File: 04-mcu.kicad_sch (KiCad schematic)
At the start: 16 parts, among them J4 USB-C, J5 microSD_PushPush, SW1 RESET, SW2 BOOT, U6 ESP32-S3-WROOM-1-N8R2

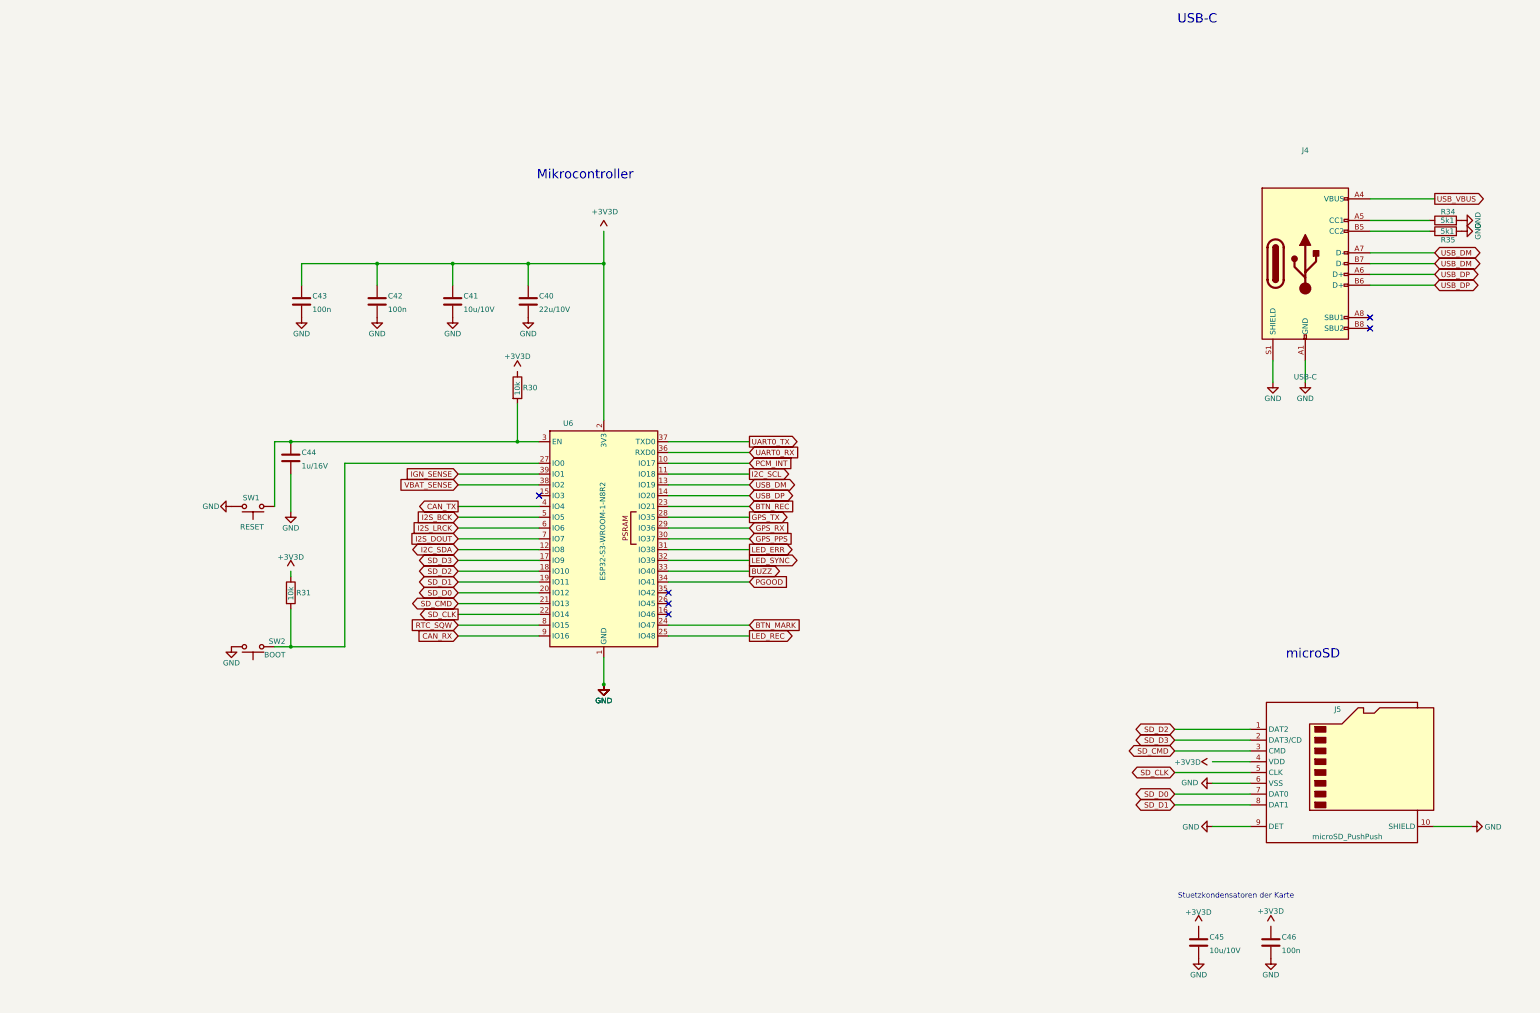
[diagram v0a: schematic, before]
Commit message: Layout verdrahten, ERC/DRC bereinigen, Werkzeugkette auf KiCad 10
Mikrofonkopf ist fertig verdrahtet (0 offene Verbindungen, 0 DRC-Fehler).
Auf der Hauptplatine bleiben 16 Verbindungen offen, ebenfalls ohne
DRC-Fehler; sie sind im interaktiven Router von KiCad zu schliessen.

Schaltplan
- 3 Speisepin-Fehler behoben (+4V6, ADC-AVDD, Uhrenbatterie brauchen ein
  Speiseflag - sie werden ueber Drossel, Ferrit bzw. Zelle gespeist und
  haben damit keine Quelle im Sinne der Regelpruefung)
- Netzname GND_CHASSIS entfernt: lag auf demselben Knoten wie GND
- TLV1117LV33 hatte einen Pin 4 fuer die Kuehlfahne, den es im Footprint
  SOT-223-3_TabPin2 nicht gibt - dort traegt Pad 2 die Fahne
- Piezo von Durchsteck- auf SMD-Ausfuehrung (Murata PKMCS0909E): fuer den
  12,5-mm-Typ gibt es keine Position, an der seine Anschluesse nicht auf
  der Gegenseite auf Pads treffen
- ERC laeuft jetzt fehlerfrei

Layout
- Durchsteckpads belegen beide Seiten. J1, J4 und J6 standen ueber
  rueckseitigen Bauteilen; das waren vier echte Kurzschluesse, unter
  anderem GPS_PPS gegen Masse an der Knopfzelle. Die eigene Pruefung
  vergleicht Durchsteckpads jetzt gegen beide Seiten, pad-genau
- In2 traegt keine Versorgungsinseln mehr, sondern Signale. Vorher wich
  der Autorouter auf die Masseflaeche aus - 140 Segmente aus 30 Netzen
  quer durch In1. Der DSN-Export kennzeichnet In1 nun als Versorgungslage
- Masseflaechen auf den Aussenlagen mit Naehvias an In1 angebunden und auf
  automatische Inselentfernung gestellt
- Netzklasse auf 0,18 mm Bahn, 0,15 mm Abstand, 0,5/0,25-mm-Via verengt;
  mit KiCads Vorgabewerten blieb rund ein Dutzend Verbindungen mehr offen
- Beschaffungsfelder unsichtbar und auf die Fab-Lage: sichtbar im
  Siebdruck ueberdecken die Herstellernummern die halbe Platine, das
  waren 151 der urspruenglich 214 Regelwarnungen

Werkzeuge
- pipeline.sh fasst den Layoutlauf zusammen
- fix_drc.py nimmt KiCads Regelpruefung als Instanz und entfernt, was sie
  beanstandet - die eigenen Abst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
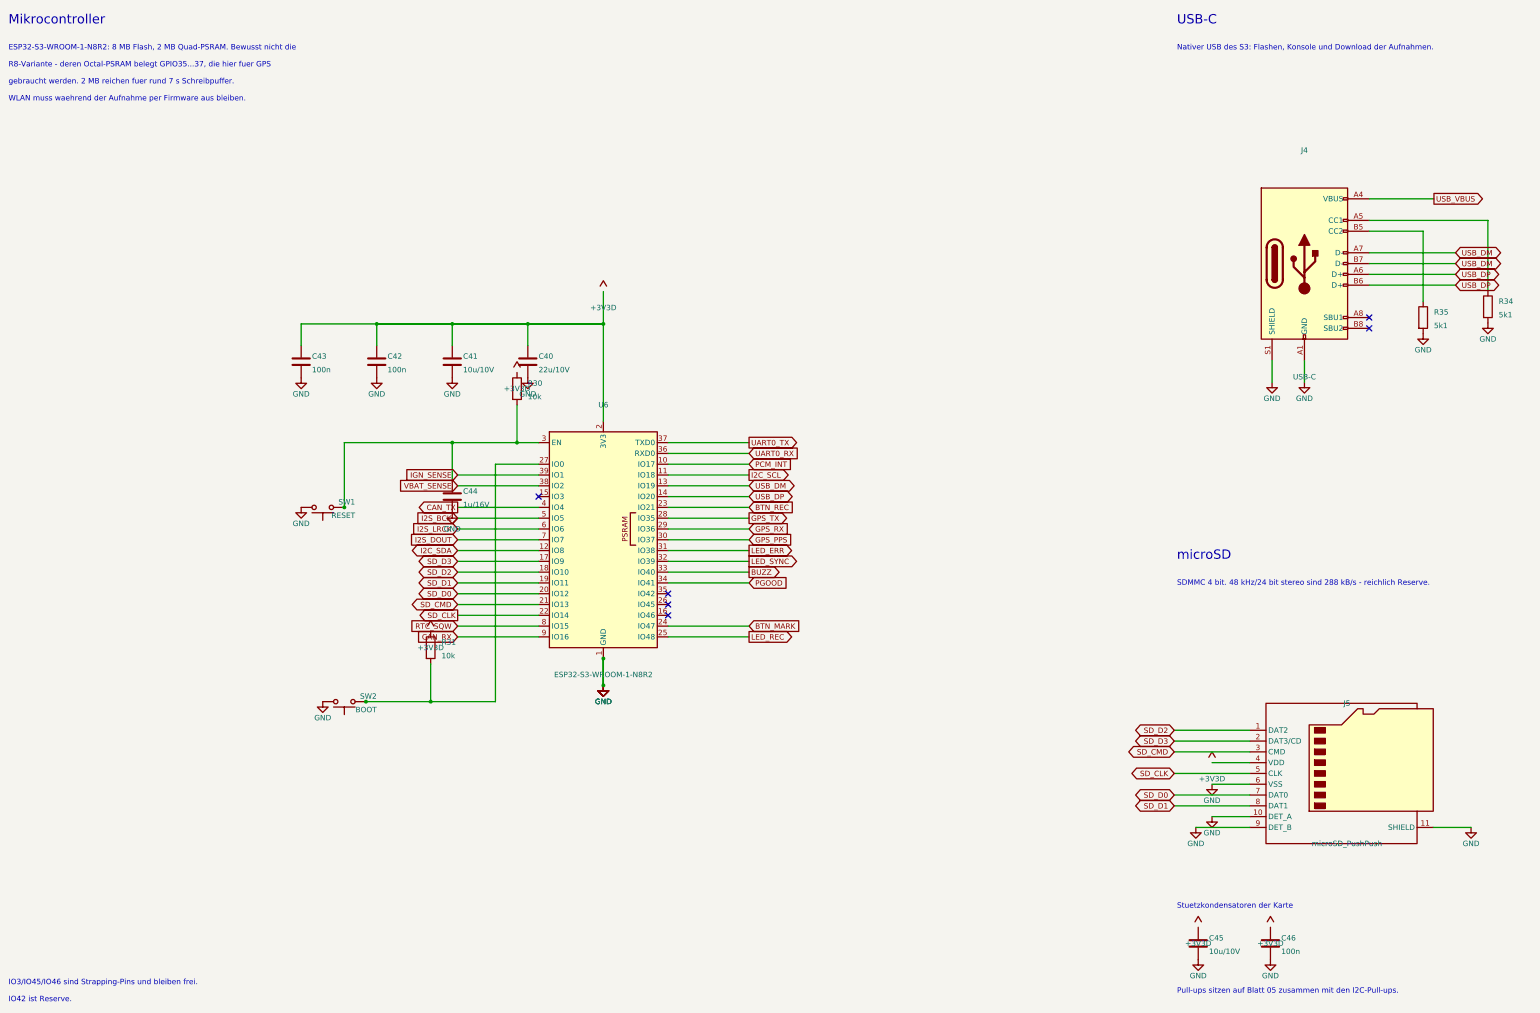
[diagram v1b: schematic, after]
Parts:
- removed J5: microSD_PushPush, Connector_Card:microSD_HC_Hirose_DM3D-SF, symbol Connector:Micro_SD_Card_Det1
- added J5: microSD_PushPush, Connector_Card:microSD_HC_Hirose_DM3D-SF, symbol Connector:Micro_SD_Card_Det2
- U6: footprint RF_Module:ESP32-S2-WROOM -> RF_Module:ESP32-S3-WROOM-1
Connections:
- net +3V3D: now also J5.4 (VDD)
- net GND: now also J5.10 (DET_A), J5.11 (SHIELD), J5.6 (VSS), J5.9 (DET_B)
- net SD_CLK: now also J5.5 (CLK)
- net SD_CMD: now also J5.3 (CMD)
- net SD_D0: now also J5.7 (DAT0)
- net SD_D1: now also J5.8 (DAT1)
- net SD_D2: now also J5.1 (DAT2)
- net SD_D3: now also J5.2 (DAT3/CD)
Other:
- note added: "ESP32-S3-WROOM-1-N8R2: 8 MB Flash, 2 MB Quad-PSRAM. Bewusst nicht die"
- note added: "IO3/IO45/IO46 sind Strapping-Pins und bleiben frei."
- note added: "IO42 ist Reserve."
- note added: "Nativer USB des S3: Flashen, Konsole und Download der Aufnahmen."
- note added: "Pull-ups sitzen auf Blatt 05 zusammen mit den I2C-Pull-ups."
- note added: "R8-Variante - deren Octal-PSRAM belegt GPIO35...37, die hier fuer GPS"
- note added: "SDMMC 4 bit. 48 kHz/24 bit stereo sind 288 kB/s - reichlich Reserve."
- note added: "WLAN muss waehrend der Aufnahme per Firmware aus bleiben."
- note added: "gebraucht werden. 2 MB reichen fuer rund 7 s Schreibpuffer."
- company: (none) -> Hayabusa / exhaust-mic
- title: ESP32-S3, USB-C und microSD -> Exhaust-Mic - ESP32-S3, USB-C und microSD
- moved on the sheet: C40, C41, C42, C43, C44, R31, R34, R35, SW1, SW2

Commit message: modified:   01-power.kicad_sch 	modified:   02-analog.kicad_sch 	modified:   03-adc.kicad_sch 	modified:   04-mcu.kicad_sch 	modified:   05-io.kicad_sch 	modified:   exhaust-mic.kicad_pcb 	modified:   exhaust-mic.kicad_pro 	modified:   exhaust-mic.kicad_sch 	modified:   mic-head/mic-head.kicad_pcb 	modified:   mic-head/mic-head.kicad_pro 	modified:   mic-head/mic-head.kicad_sch 	new file:   ~exhaust-mic.kicad_pro.lck
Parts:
- removed J5: microSD_PushPush, Connector_Card:microSD_HC_Hirose_DM3D-SF, symbol Connector:Micro_SD_Card_Det2
- added J5: microSD_PushPush, Connector_Card:microSD_HC_Hirose_DM3D-SF, symbol Connector:Micro_SD_Card_Det1
- U6: footprint RF_Module:ESP32-S3-WROOM-1 -> RF_Module:ESP32-S2-WROOM
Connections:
- net +3V3D: now also J5.4 (VDD)
- net GND: now also J5.10 (SHIELD), J5.6 (VSS), J5.9 (DET)
- net SD_CLK: now also J5.5 (CLK)
- net SD_CMD: now also J5.3 (CMD)
- net SD_D0: now also J5.7 (DAT0)
- net SD_D1: now also J5.8 (DAT1)
- net SD_D2: now also J5.1 (DAT2)
- net SD_D3: now also J5.2 (DAT3/CD)
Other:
- note removed: "ESP32-S3-WROOM-1-N8R2: 8 MB Flash, 2 MB Quad-PSRAM. Bewusst nicht die"
- note removed: "IO3/IO45/IO46 sind Strapping-Pins und bleiben frei."
- note removed: "IO42 ist Reserve."
- note removed: "Nativer USB des S3: Flashen, Konsole und Download der Aufnahmen."
- note removed: "Pull-ups sitzen auf Blatt 05 zusammen mit den I2C-Pull-ups."
- note removed: "R8-Variante - deren Octal-PSRAM belegt GPIO35...37, die hier fuer GPS"
- note removed: "SDMMC 4 bit. 48 kHz/24 bit stereo sind 288 kB/s - reichlich Reserve."
- note removed: "WLAN muss waehrend der Aufnahme per Firmware aus bleiben."
- note removed: "gebraucht werden. 2 MB reichen fuer rund 7 s Schreibpuffer."
- company: Hayabusa / exhaust-mic -> (none)
- title: Exhaust-Mic - ESP32-S3, USB-C und microSD -> ESP32-S3, USB-C und microSD
- moved on the sheet: C40, C41, C42, C43, C44, R31, R34, R35, SW1, SW2
